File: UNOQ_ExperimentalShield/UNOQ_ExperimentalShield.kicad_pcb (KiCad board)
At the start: 4 copper layers, 68.6 x 53.3 mm, 117 parts, among them CN1 485, CN2 USB, CN3 Can, CN4 Can, CN5 485, J1 Power, J2 Digital/PWM, J3 Analog, J4 Digital/PWM, Q2 SS8050, SW1 Usr1, SW2 Usr1, SW3 Usr1, SW4 Usr1, U1 25LCxxx, U2 LM35-D, U3 MAX3485EESA+T, U4 CH340N, U5 TJA1051T-3

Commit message: minor
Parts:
- removed JP6: RS485 Term, Connector_PinHeader_2.54mm:PinHeader_1x02_P2.54mm_Vertical
- removed R15, R16, R17, R79: 1k, Resistor_SMD:R_0402_1005Metric
- added kibuzzard-694288F9: G***, kibuzzard-694288F9, F.Cu at (122.6, 97.0)
- added kibuzzard-69428907: G***, kibuzzard-69428907, F.Cu at (119.4, 97.1)
- JP5: value RS485 Term -> Jmp; footprint Connector_PinHeader_2.54mm:PinHeader_1x02_P2.54mm_Vertical -> Connector_PinHeader_2.54mm:PinHeader_2x02_P2.54mm_Vertical
- moved kibuzzard-693AAC3D 6.57 mm to (145.4, 84.3), turned to 0 degrees
- moved kibuzzard-693AAC4C 6.23 mm to (157.9, 84.2), turned to 0 degrees
- moved kibuzzard-693AAC1A 1.18 mm to (117.1, 92.4)
- moved JP5 0.58 mm to (115.8, 87.3), turned to 0 degrees
- moved kibuzzard-693AAC2B 0.53 mm to (117.1, 84.7)
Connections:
- net /B renamed /485_T_B
- net Net-(JP5-B) renamed /485_T_A
- R27 pad 2: Net-(JP6-B) -> /CAN_T_H
- RV1 pad 1: Net-(R79-Pad2) -> +3V3
- RV1 pad 3: Net-(R15-Pad1) -> GND
- RV2 pad 1: Net-(R16-Pad2) -> +3V3
- RV2 pad 3: Net-(R17-Pad1) -> GND
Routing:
- net +3V3: track 201.6 -> 210.0 mm
- net /485_T_B: track 53.2 -> 45.7 mm
- net Net-(R79-Pad2): track 6.79 -> 0.00 mm
- net Net-(R17-Pad1): track 6.47 -> 0.00 mm
- net Net-(R16-Pad2): track 6.32 -> 0.00 mm
- net Net-(R15-Pad1): track 5.88 -> 0.00 mm
- net /CAN_T_H: track 0.00 -> 3.16 mm
- net Net-(JP6-B): track 3.05 -> 0.00 mm
- net GND: track 59.6 -> 57.4 mm, vias 123 -> 120
- net /A0: track 7.38 -> 9.09 mm

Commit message: minor
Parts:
- added C5: 100nF, Capacitor_SMD:C_0402_1005Metric, F.Cu at (119.6, 81.6)
- added kibuzzard-69443E17: G***, kibuzzard-69443E17, B.Cu at (103.5, 67.0)
- added kibuzzard-69443E38: G***, kibuzzard-69443E38, B.Cu at (103.6, 70.6)
- added kibuzzard-69443E67: G***, kibuzzard-69443E67, B.Cu at (102.5, 77.6)
- added kibuzzard-69443E7E: G***, kibuzzard-69443E7E, B.Cu at (102.5, 81.1)
- moved C4 45.5 mm to (164.5, 74.6), turned to 180 degrees
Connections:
- C4 pad 1: +3V3 -> +5V
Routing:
- net +5V: track 83.6 -> 92.6 mm, vias 2 -> 4
- net /VBUS: track 0.00 -> 8.70 mm, vias 0 -> 2
- net /485_T_B: track 45.7 -> 52.7 mm

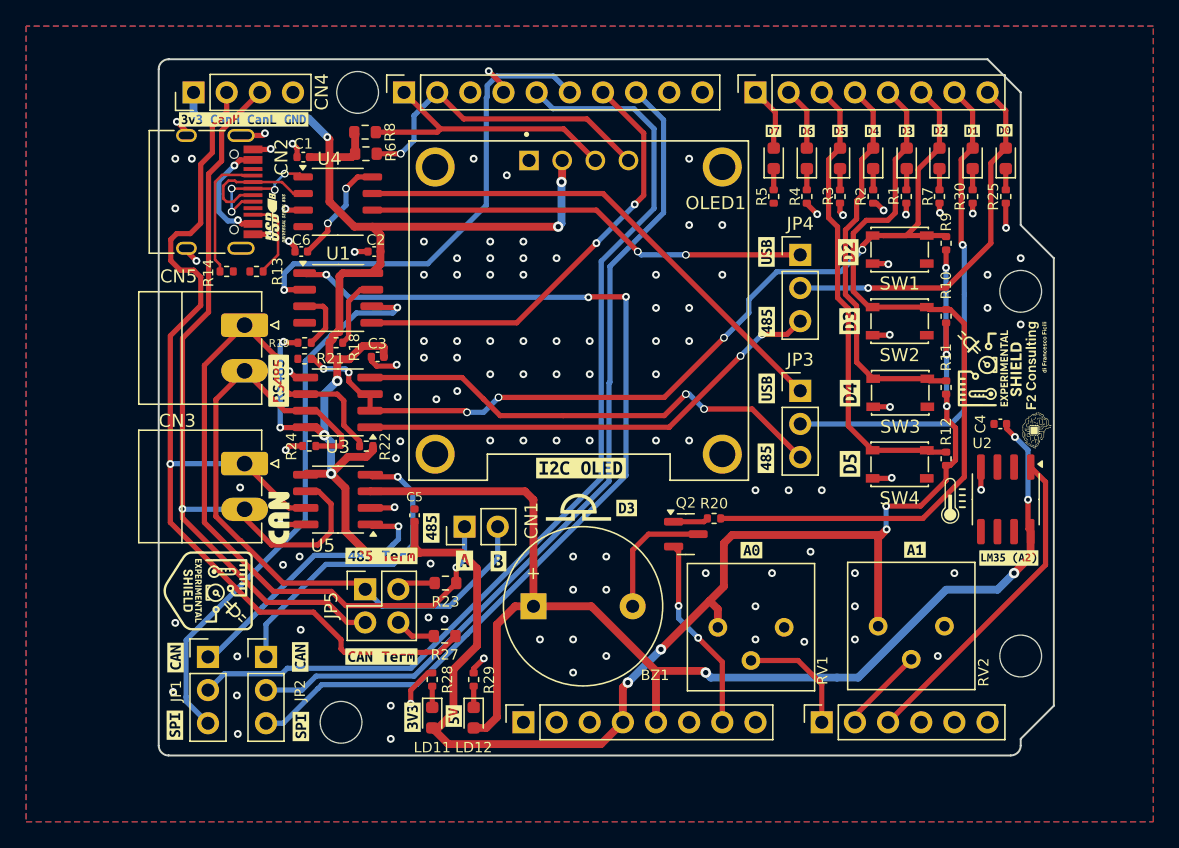
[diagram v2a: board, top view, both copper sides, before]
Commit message: Some fixes: - Fixed labesl dimension - Fixed resistor values for leds - Fixed OLED footprint - Added HW version
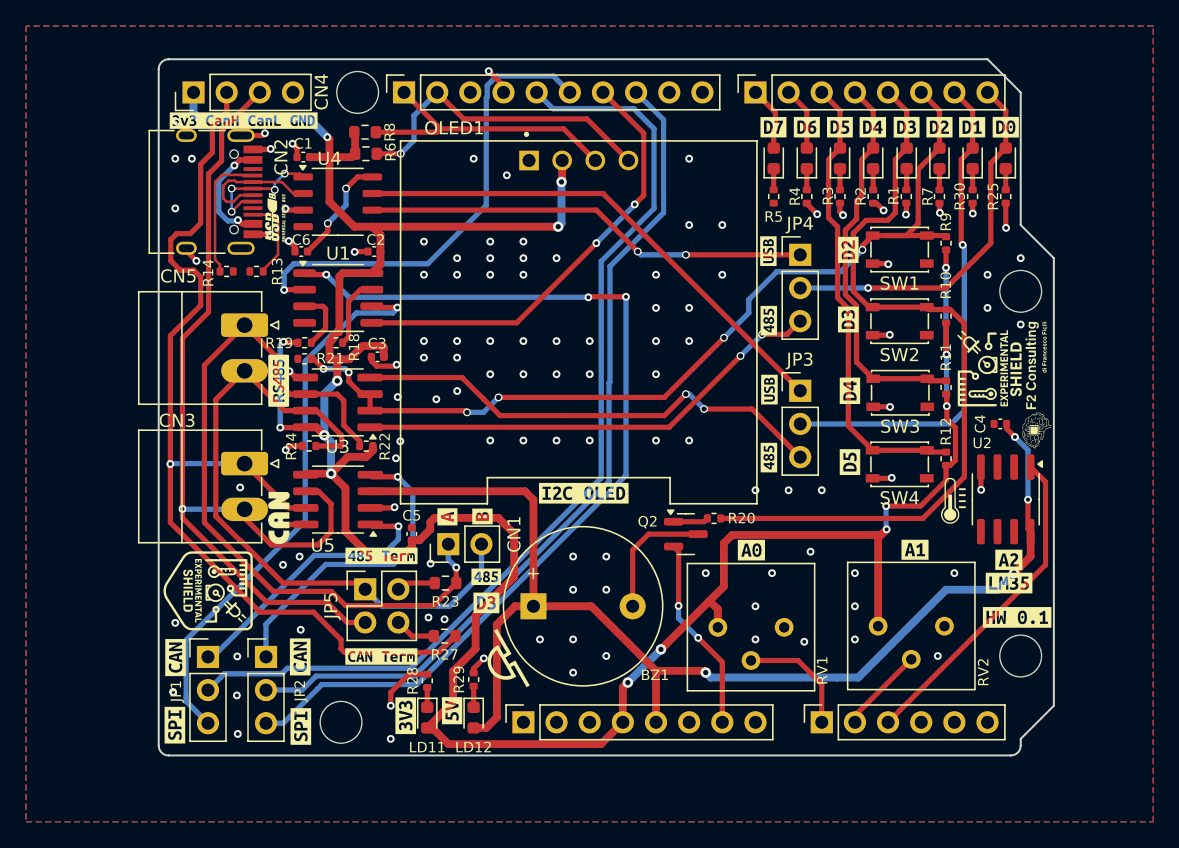
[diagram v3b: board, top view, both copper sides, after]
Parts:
- removed kibuzzard-693AAA50: G***, kibuzzard-693AAA50
- removed kibuzzard-693AAA96: G***, kibuzzard-693AAA96
- removed kibuzzard-693AAA9D: G***, kibuzzard-693AAA9D
- removed kibuzzard-693AAAA3: G***, kibuzzard-693AAAA3
- removed kibuzzard-693AAB49: G***, kibuzzard-693AAB49
- removed kibuzzard-693AAB75: G***, kibuzzard-693AAB75
- removed kibuzzard-693AAB7A: G***, kibuzzard-693AAB7A
- removed kibuzzard-693AAB7F: G***, kibuzzard-693AAB7F
- removed kibuzzard-693AAB85: G***, kibuzzard-693AAB85
- removed kibuzzard-693AAB97: G***, kibuzzard-693AAB97
- removed kibuzzard-693AAB9C: G***, kibuzzard-693AAB9C
- removed kibuzzard-693AABA1: G***, kibuzzard-693AABA1
- removed kibuzzard-693AABC4 (x2): G***, kibuzzard-693AABC4
- removed kibuzzard-693AABCF (x2): G***, kibuzzard-693AABCF
- removed kibuzzard-693AABED (x2): G***, kibuzzard-693AABED
- removed kibuzzard-693AABF8 (x2): G***, kibuzzard-693AABF8
- removed kibuzzard-693AAC1A: G***, kibuzzard-693AAC1A
- removed kibuzzard-693AAC2B: G***, kibuzzard-693AAC2B
- removed kibuzzard-693AAC3D: G***, kibuzzard-693AAC3D
- removed kibuzzard-693AAC4C: G***, kibuzzard-693AAC4C
- removed kibuzzard-693AAD0C: G***, kibuzzard-693AAD0C
- removed kibuzzard-693AB116: G***, kibuzzard-693AB116
- removed kibuzzard-693AB11F: G***, kibuzzard-693AB11F
- removed kibuzzard-693AB138: G***, kibuzzard-693AB138
- removed kibuzzard-693AB2E8: G***, kibuzzard-693AB2E8
- removed kibuzzard-693AC547: G***, kibuzzard-693AC547
- removed kibuzzard-694288F9: G***, kibuzzard-694288F9
- removed kibuzzard-69428907: G***, kibuzzard-69428907
- removed kibuzzard-69443E17: G***, kibuzzard-69443E17
- added kibuzzard-69595B90: G***, kibuzzard-69595B90, F.Cu at (164.9, 51.9)
- added kibuzzard-69595B9D: G***, kibuzzard-69595B9D, F.Cu at (162.3, 51.9)
- added kibuzzard-69595BB4: G***, kibuzzard-69595BB4, F.Cu at (159.8, 51.9)
- added kibuzzard-69595BC0: G***, kibuzzard-69595BC0, F.Cu at (157.3, 51.9)
- added kibuzzard-69595BCB: G***, kibuzzard-69595BCB, F.Cu at (154.7, 51.9)
- added kibuzzard-69595BD4: G***, kibuzzard-69595BD4, F.Cu at (152.2, 51.9)
- added kibuzzard-69595BDC: G***, kibuzzard-69595BDC, F.Cu at (149.7, 51.9)
- added kibuzzard-69595BE4: G***, kibuzzard-69595BE4, F.Cu at (147.1, 51.9)
- added kibuzzard-69595BF0: G***, kibuzzard-69595BF0, F.Cu at (152.8, 61.3)
- added kibuzzard-69595BF8: G***, kibuzzard-69595BF8, F.Cu at (152.8, 66.6)
- added kibuzzard-69595C06: G***, kibuzzard-69595C06, F.Cu at (153.0, 72.1)
- added kibuzzard-69595C0F: G***, kibuzzard-69595C0F, F.Cu at (153.0, 77.5)
- added kibuzzard-69595C48: G***, kibuzzard-69595C48, F.Cu at (165.1, 85.0)
- added kibuzzard-69595C56: G***, kibuzzard-69595C56, F.Cu at (165.2, 86.8)
- added kibuzzard-69595C5E: G***, kibuzzard-69595C5E, F.Cu at (145.4, 84.3)
- added kibuzzard-69595C64: G***, kibuzzard-69595C64, F.Cu at (157.9, 84.2)
- added kibuzzard-69595C6D: G***, kibuzzard-69595C6D, F.Cu at (125.1, 88.3)
- added kibuzzard-69595C77: G***, kibuzzard-69595C77, B.Cu at (103.5, 67.0)
- added kibuzzard-69595C82: G***, kibuzzard-69595C82, F.Cu at (110.8, 92.5)
- added kibuzzard-69595C87: G***, kibuzzard-69595C87, F.Cu at (110.9, 97.8)
- added kibuzzard-69595C8D: G***, kibuzzard-69595C8D, F.Cu at (101.3, 92.5)
- added kibuzzard-69595C92: G***, kibuzzard-69595C92, F.Cu at (101.2, 97.7)
- added kibuzzard-69595C98: G***, kibuzzard-69595C98, F.Cu at (118.9, 97.0)
- added kibuzzard-69595CA1: G***, kibuzzard-69595CA1, F.Cu at (122.5, 96.6)
- added kibuzzard-69595CF0: G***, kibuzzard-69595CF0, F.Cu at (122.1, 81.7)
- added kibuzzard-69595CF5: G***, kibuzzard-69595CF5, F.Cu at (124.8, 81.7)
- added kibuzzard-69595D08: G***, kibuzzard-69595D08, F.Cu at (106.5, 51.4)
- added kibuzzard-69595D77: G***, kibuzzard-69595D77, F.Cu at (117.1, 84.7)
- added kibuzzard-69595D7B: G***, kibuzzard-69595D7B, F.Cu at (117.1, 92.4)
- added kibuzzard-69595D81: G***, kibuzzard-69595D81, F.Cu at (125.1, 86.3)
- added kibuzzard-695F89C6: G***, kibuzzard-695F89C6, F.Cu at (165.8, 89.4)
- added kibuzzard-695F8C20: G***, kibuzzard-695F8C20, F.Cu at (146.7, 66.7)
- added kibuzzard-695F8C29: G***, kibuzzard-695F8C29, F.Cu at (146.8, 72.0)
- added kibuzzard-695F8C32: G***, kibuzzard-695F8C32, F.Cu at (146.8, 77.2)
- added kibuzzard-695F8C3A: G***, kibuzzard-695F8C3A, F.Cu at (146.7, 61.4)
- OLED1: footprint oled:MODULE_DM-OLED096-636 -> oled:OLED096
- R1, R2, R25, R3, R30, R4, R5, R7: value 330 -> 1k
- moved G*** 13.4 mm to (126.3, 93.0), turned to 120 degrees
- moved kibuzzard-693AADEF 1.94 mm to (132.6, 79.9)
- moved CN1 1.83 mm to (122.2, 83.8)
- moved C5 1.45 mm to (119.4, 83.0)
- moved R28 0.39 mm to (120.6, 94.3)
- moved LD11 0.38 mm to (120.6, 97.1)
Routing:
- net +3V3: track 210.3 -> 215.7 mm
- net /485_T_B: track 52.7 -> 50.8 mm
- net /A: track 58.7 -> 57.4 mm
- net GND: track 57.4 -> 58.6 mm, vias 120 -> 119

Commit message: Some modifications: - TX/RX Led polarity inverted - LM35 has been replaced with TMP102 (I2C Thermo, better and cheaper) - OLED Shape has been fixed - LED Resistors updated to 1k
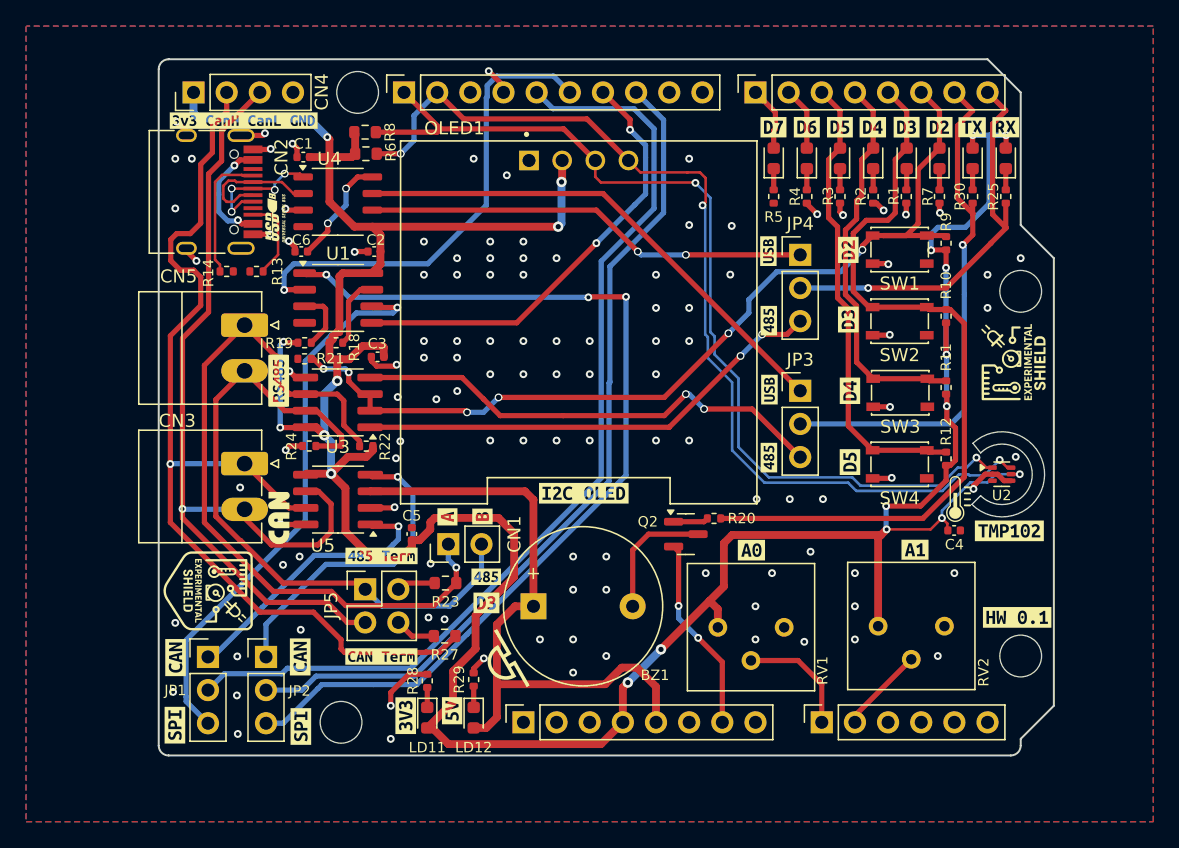
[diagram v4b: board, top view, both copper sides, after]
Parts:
- removed the G*** at (167.3, 71.6)
- removed kibuzzard-69595B90: G***, kibuzzard-69595B90
- removed kibuzzard-69595B9D: G***, kibuzzard-69595B9D
- removed kibuzzard-69595C48: G***, kibuzzard-69595C48
- removed kibuzzard-69595C56: G***, kibuzzard-69595C56
- added kibuzzard-69764F79: G***, kibuzzard-69764F79, F.Cu at (165.2, 82.8)
- added kibuzzard-69765506: G***, kibuzzard-69765506, F.Cu at (162.3, 51.9)
- added kibuzzard-6976550D: G***, kibuzzard-6976550D, F.Cu at (164.9, 51.9)
- U2: value LM35-D -> TMP102xxDRL; footprint Package_SO:SOIC-8_3.9x4.9mm_P1.27mm -> Package_TO_SOT_SMD:SOT-563
- moved C4 8.89 mm to (160.9, 82.8), turned to 0 degrees
- moved U2 1.95 mm to (164.6, 78.5), turned to 0 degrees
- moved G*** 1.89 mm to (165.5, 69.8)
- moved G*** 0.41 mm to (161.3, 80.3)
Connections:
- C4 pad 1: +5V -> +3V3
- LD10 pad 2: /TX/D1 -> +3V3
- LD9 pad 2: /RX/D0 -> +3V3
- R25 pad 2: GND -> /RX/D0
- R30 pad 2: GND -> /TX/D1
- U2 pad 1: /A2 -> /SCL/A5
- U2 pad 2: unconnected-(U2-NC-Pad2) -> GND
- U2 pad 5: unconnected-(U2-NC-Pad5) -> +3V3
- U2 pad 6: unconnected-(U2-NC-Pad6) -> /SDA/A4
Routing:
- net /SCL/A5: track 21.9 -> 74.5 mm, vias 0 -> 2
- net /SDA/A4: track 24.5 -> 76.8 mm, vias 1 -> 3
- net +5V: track 92.6 -> 49.6 mm, vias 4 -> 0
- net +3V3: track 215.7 -> 247.4 mm, vias 15 -> 20
- net /A2: track 25.0 -> 0.00 mm
- net /RX/D0: track 28.6 -> 31.4 mm
- net /TX/D1: track 38.4 -> 40.1 mm
- net GND: track 58.6 -> 57.8 mm, vias 119 -> 117
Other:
- outline, holes or cut-outs redrawn

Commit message: final vesion
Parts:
- removed BZ1: Buzzer, Buzzer_Beeper:Buzzer_12x9.5RM7.6
- removed the G*** at (126.3, 93.0)
- removed Q2: SS8050, Package_TO_SOT_SMD:SOT-23
- removed R20: 1k, Resistor_SMD:R_0402_1005Metric
- removed kibuzzard-69595BCB: G***, kibuzzard-69595BCB
- removed kibuzzard-69595BD4: G***, kibuzzard-69595BD4
- removed kibuzzard-69595BDC: G***, kibuzzard-69595BDC
- removed kibuzzard-69595BE4: G***, kibuzzard-69595BE4
- removed kibuzzard-69595C06: G***, kibuzzard-69595C06
- removed kibuzzard-69595C0F: G***, kibuzzard-69595C0F
- removed kibuzzard-69595C6D: G***, kibuzzard-69595C6D
- removed kibuzzard-69595D08: G***, kibuzzard-69595D08
- added JP6: Jmp, Connector_PinHeader_2.54mm:PinHeader_1x03_P2.54mm_Vertical, F.Cu at (132.3, 89.9)
- added JP7: Jmp, Connector_PinHeader_2.54mm:PinHeader_1x03_P2.54mm_Vertical, F.Cu at (136.0, 89.9)
- added JP8: Jmp, Connector_PinHeader_2.54mm:PinHeader_1x03_P2.54mm_Vertical, F.Cu at (139.6, 84.8)
- added LD7: Rx, LED_SMD:LED_0603_1608Metric, F.Cu at (132.3, 93.8)
- added LD8: Tx, LED_SMD:LED_0603_1608Metric, F.Cu at (135.6, 93.8)
- added R15: 1k, Resistor_SMD:R_0402_1005Metric, F.Cu at (129.5, 93.8)
- added R16: 1k, Resistor_SMD:R_0402_1005Metric, F.Cu at (138.4, 93.7)
- added kibuzzard-697C896A: G***, kibuzzard-697C896A, F.Cu at (154.7, 51.9)
- added kibuzzard-697C8970: G***, kibuzzard-697C8970, F.Cu at (152.2, 51.9)
- added kibuzzard-697C8977: G***, kibuzzard-697C8977, F.Cu at (149.7, 51.9)
- added kibuzzard-697C897C: G***, kibuzzard-697C897C, F.Cu at (147.1, 51.9)
- added kibuzzard-697C8A8B: G***, kibuzzard-697C8A8B, F.Cu at (153.0, 72.1)
- added kibuzzard-697C8A92: G***, kibuzzard-697C8A92, F.Cu at (153.0, 77.5)
- added kibuzzard-697C8D01: G***, kibuzzard-697C8D01, F.Cu at (132.3, 95.3)
- added kibuzzard-697C8D0C: G***, kibuzzard-697C8D0C, F.Cu at (135.8, 95.3)
- added kibuzzard-698784C3: G***, kibuzzard-698784C3, F.Cu at (142.2, 89.9)
- added kibuzzard-698784D4: G***, kibuzzard-698784D4, F.Cu at (142.2, 84.9)
- added kibuzzard-69878868: G***, kibuzzard-69878868, F.Cu at (128.9, 84.8)
- added kibuzzard-6987886F: G***, kibuzzard-6987886F, F.Cu at (128.5, 89.9)
- added kibuzzard-6987894B: G***, kibuzzard-6987894B, F.Cu at (106.0, 95.6)
- added kibuzzard-69878B44: G***, kibuzzard-69878B44, F.Cu at (106.5, 51.4)
- CN3, CN5: footprint Connector_Phoenix_MC:PhoenixContact_MC_1,5_2-G-3.5_1x02_P3.50mm_Horizontal -> TerminalBlock_Phoenix:TerminalBlock_Phoenix_MPT-0,5-2-2.54_1x02_P2.54mm_Horizontal
- U3: value MAX3485EESA+T -> MAX3485ESA-MS
- kibuzzard-69443E38, kibuzzard-69443E67, kibuzzard-69443E7E, kibuzzard-69595C77: moved to F.Cu
- moved kibuzzard-69443E67 6.63 mm to (108.8, 75.5), turned to 90 degrees
- moved G*** 6.48 mm to (102.7, 81.7), turned to 0 degrees
- moved kibuzzard-69443E7E 6.46 mm to (108.8, 79.6), turned to 90 degrees
- moved G*** 6.42 mm to (102.8, 72.3), turned to 0 degrees
- moved kibuzzard-69443E38 5.50 mm to (109.0, 69.6), turned to -90 degrees
- moved kibuzzard-69595C77 5.48 mm to (109.0, 66.6), turned to -90 degrees
- moved RV1 3.02 mm to (145.9, 90.1)
- moved kibuzzard-69595C5E 2.71 mm to (148.1, 84.1)
- moved CN3 2.62 mm to (104.4, 76.1)
- moved kibuzzard-695F89C6 2.49 mm to (167.2, 87.4), turned to -90 degrees
- moved CN5 2.16 mm to (104.4, 66.7)
- moved RV2 1.04 mm to (156.2, 90.1)
- moved G*** 0.85 mm to (104.0, 86.5)
- moved kibuzzard-69595C64 0.81 mm to (158.8, 84.2)
- moved G*** 0.72 mm to (165.5, 70.6)
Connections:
- C1 pad 1: +3V3 -> /Vio
- C2 pad 1: +3V3 -> /Vio
- C3 pad 1: +3V3 -> /Vio
- C5 pad 1: +3V3 -> +5V
- CN4 pad 1: +3V3 -> /Vio
- J4 pad 3: /D5* -> /D5*/FDCAN_RX
- J4 pad 4: /D4 -> /D4/FDCAN_TX
- JP1 pad 1: /CANTX -> /CANTX_R4
- JP2 pad 1: /CANRX -> /CANRX_R4
- LD3 pad 2: /D4 -> /D6*
- LD4 pad 2: /D5* -> /D7
- LD5 pad 2: /D6* -> /D8
- LD6 pad 2: /D7 -> /D9*
- R11 pad 2: /D4 -> /D6*
- R12 pad 2: /D5* -> /D7
- SW3 pad 2: /D4 -> /D6*
- SW4 pad 2: /D5* -> /D7
- U1 pad 8: +3V3 -> /Vio
- U3 pad 8: +3V3 -> /Vio
- U4 pad 5: +3V3 -> /Vio
- U5 pad 5: +3V3 -> /Vio
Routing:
- net /Vio: track 0.00 -> 94.4 mm, vias 0 -> 11
- net /D5*/FDCAN_RX: track 0.00 -> 54.0 mm
- net /D4/FDCAN_TX: track 0.00 -> 51.4 mm
- net /D5*: track 35.4 -> 0.00 mm
- net /CANTX_R4: track 0.00 -> 35.3 mm, vias 0 -> 1
- net /D7: track 4.95 -> 39.5 mm
- net /D3*: track 59.8 -> 26.2 mm
- net /D4: track 29.9 -> 0.00 mm
- net /D6*: track 4.85 -> 34.1 mm
- net /CANRX_R4: track 0.00 -> 25.2 mm, vias 0 -> 1
- net +3V3: track 247.4 -> 229.9 mm, vias 20 -> 16
- net +5V: track 49.6 -> 65.4 mm, vias 0 -> 4
- net GND: track 57.8 -> 42.8 mm, vias 117 -> 165
- net /CANTX: track 21.5 -> 35.6 mm, vias 1 -> 2
- net /D8: track 0.00 -> 10.3 mm
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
